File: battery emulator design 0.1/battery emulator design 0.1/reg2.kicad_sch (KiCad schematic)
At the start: 12 parts, among them U3 LM741, U4 LM317_TO-220

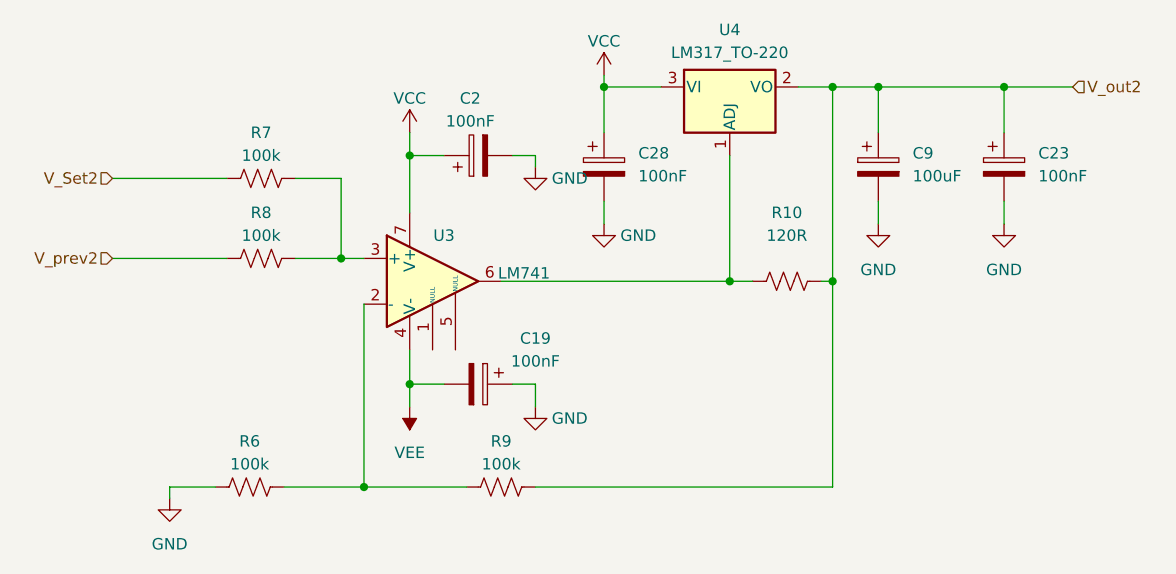
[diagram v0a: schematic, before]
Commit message: added pots to voltage buffers, other minor changes
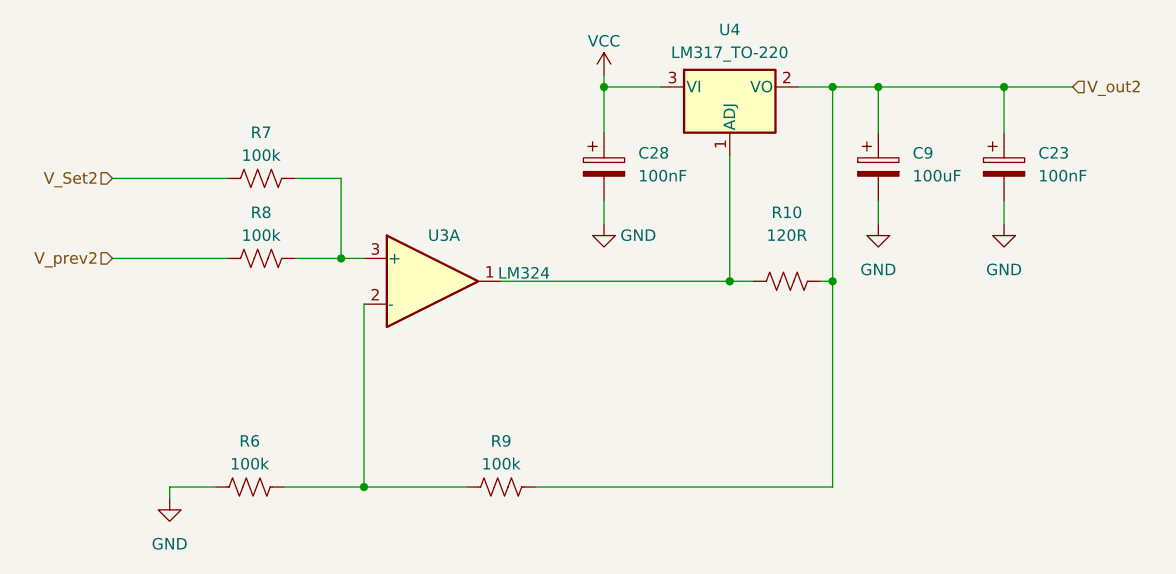
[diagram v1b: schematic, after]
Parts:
- removed C19, C2: 100nF, Capacitor_THT:C_Disc_D3.4mm_W2.1mm_P2.50mm, symbol Device:C_Polarized
- U3: value LM741 -> LM324; symbol Amplifier_Operational:LM741 -> Amplifier_Operational:LM324
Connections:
- net VCC: no longer U3.7 (V+)
- net at R10.2, U4.1 (ADJ): now also U3.1; no longer U3.6
- removed net VEE: U3.4 (V-)
